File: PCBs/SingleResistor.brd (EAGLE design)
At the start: 14.5 x 42 mm, 3 parts

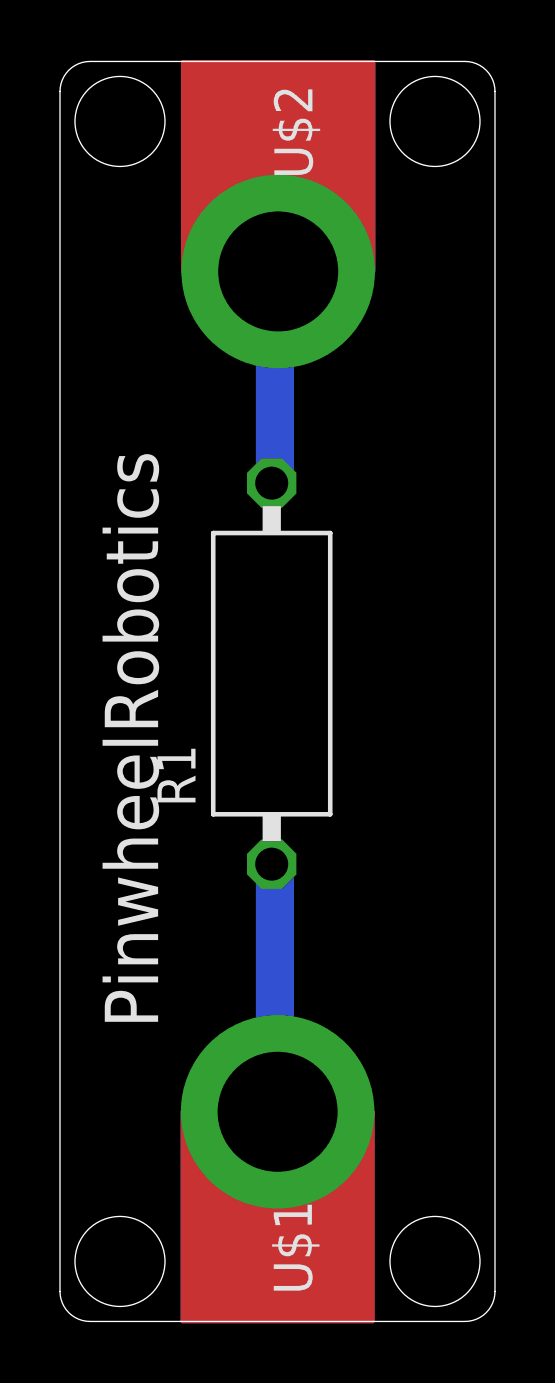
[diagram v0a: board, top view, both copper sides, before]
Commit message: Update for Dim width is 42 length is 28 for type 2 pcb
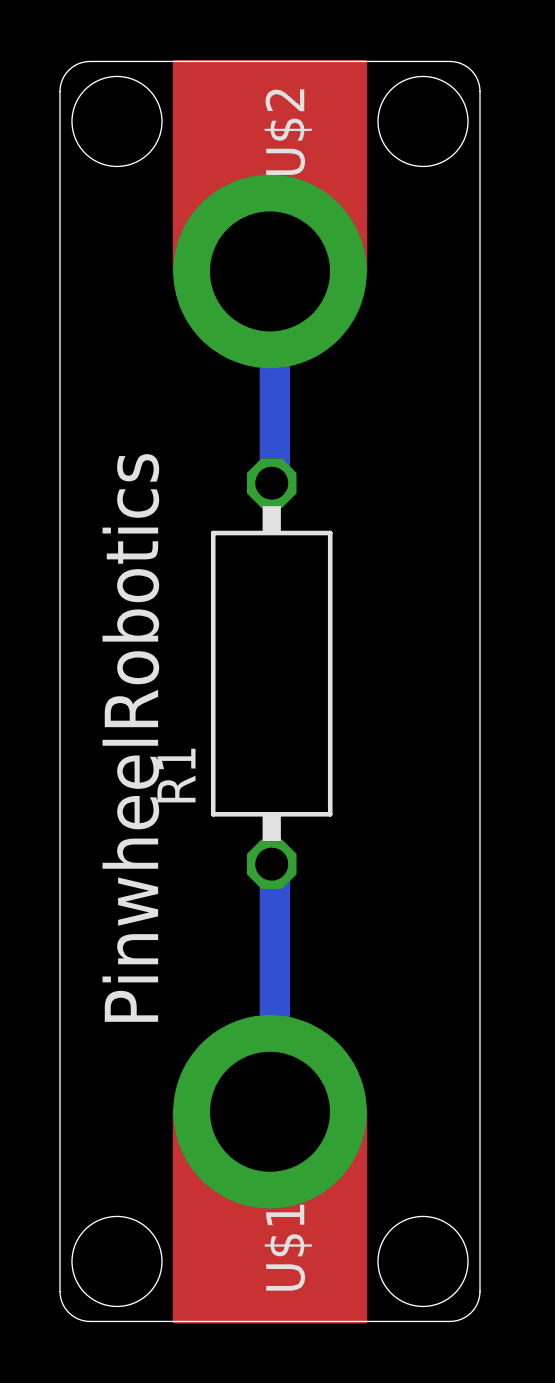
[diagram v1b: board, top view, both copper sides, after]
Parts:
- moved U$2 0.27 mm to (7.00, 35.0)
- moved U$1 0.25 mm to (7.00, 6.99)
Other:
- board size 14.5 x 42 mm -> 14 x 42 mm
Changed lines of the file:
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@@
 <drawing>
 <settings>
-<setting alwaysvectorfont="no"/>
+<setting alwaysvectorfont="yes"/>
 <setting verticaltext="up"/>
 </settings>
@@
 <board>
 <plain>
-<wire x1="1" y1="0" x2="13.5" y2="0" width="0" layer="20"/>
-<wire x1="13.5" y1="0" x2="14.5" y2="1" width="0" layer="20" curve="90"/>
-<wire x1="14.5" y1="1" x2="14.5" y2="41" width="0" layer="20"/>
-<wire x1="14.5" y1="41" x2="13.5" y2="42" width="0" layer="20" curve="90"/>
-<wire x1="13.5" y1="42" x2="1" y2="42" width="0" layer="20"/>
+<wire x1="13" y1="42" x2="1" y2="42" width="0" layer="20"/>
 <wire x1="1" y1="42" x2="0" y2="41" width="0" layer="20" curve="90"/>
 <wire x1="0" y1="41" x2="0" y2="1" width="0" layer="20"/>
 <wire x1="0" y1="1" x2="1" y2="0" width="0" layer="20" curve="90"/>
-<hole x="2" y="40" drill="3"/>
-<hole x="12.5" y="40" drill="3"/>
-<hole x="2" y="2" drill="3"/>
-<hole x="12.5" y="2" drill="3"/>
+<wire x1="1" y1="0" x2="13" y2="0" width="0" layer="20"/>
+<wire x1="13" y1="0" x2="14" y2="1" width="0" layer="20" curve="90"/>
+<wire x1="14" y1="1" x2="14" y2="41" width="0" layer="20"/>
+<wire x1="14" y1="41" x2="13" y2="42" width="0" layer="20" curve="90"/>
+<hole x="1.9" y="40" drill="3"/>
+<hole x="12.1" y="40" drill="3"/>
+<hole x="1.9" y="2" drill="3"/>
+<hole x="12.1" y="2" drill="3"/>
 <text x="3.271" y="9.772" size="1.778" layer="21" rot="R90">PinwheelRobotics</text>
 <text x="12.509" y="29.939" size="1.778" layer="22" rot="MR270">care@pinwheel.in</text>
-<dimension x1="-1" y1="42" x2="-1" y2="0" x3="-2.5" y3="21" textsize="1.778" layer="1"/>
-<dimension x1="0" y1="42.5" x2="14.5" y2="42.5" x3="7.25" y3="44" textsize="1.778" layer="1"/>
 </plain>
 <attributes>
@@
 <attribute name="VALUE" x="7.693" y="17.148" size="1.27" layer="27" ratio="10" rot="R90"/>
 </element>
-<element name="U$2" library="microbit" package="MICROBIT_PAD" value="MICROBIT_PAD" x="7.273" y="35" smashed="yes" rot="R180">
-<attribute name="NAME" x="7.146" y="41.223" size="1.27" layer="21" rot="R270"/>
+<element name="U$2" library="microbit" package="MICROBIT_PAD" value="MICROBIT_PAD" x="7" y="35" smashed="yes" rot="R180">
+<attribute name="NAME" x="6.873" y="41.223" size="1.27" layer="21" rot="R270"/>
 </element>
-<element name="U$1" library="microbit" package="MICROBIT_PAD" value="MICROBIT_PAD" x="7.254" y="6.988" smashed="yes">
-<attribute name="NAME" x="8.397" y="0.892" size="1.27" layer="21" rot="R90"/>
+<element name="U$1" library="microbit" package="MICROBIT_PAD" value="MICROBIT_PAD" x="7" y="6.988" smashed="yes">
+<attribute name="NAME" x="8.143" y="0.892" size="1.27" layer="21" rot="R90"/>
 </element>
 </elements>
@@
 <contactref element="R1" pad="1"/>
 <contactref element="U$1" pad="PAD"/>
-<wire x1="7.1628" y1="7.0104" x2="7.1628" y2="15.24" width="1.27" layer="16"/>
+<wire x1="7.1628" y1="7.0104" x2="7.1628" y2="15.24" width="1.016" layer="16"/>
 <wire x1="7.1628" y1="15.24" x2="7.058" y2="15.243" width="0.1524" layer="16"/>
-<wire x1="7.1628" y1="7.0104" x2="7.254" y2="6.988" width="0.1524" layer="16"/>
+<wire x1="7.1628" y1="7.0104" x2="7" y2="6.988" width="0.1524" layer="16"/>
 </signal>
 <signal name="N$2">
 <contactref element="U$2" pad="PAD"/>
 <contactref element="R1" pad="2"/>
-<wire x1="7.1628" y1="34.8996" x2="7.1628" y2="28.0416" width="1.27" layer="16"/>
+<wire x1="7.1628" y1="34.8996" x2="7.1628" y2="28.0416" width="1.016" layer="16"/>
 <wire x1="7.1628" y1="28.0416" x2="7.058" y2="27.943" width="0.1524" layer="16"/>
-<wire x1="7.1628" y1="34.8996" x2="7.273" y2="35" width="0.1524" layer="16"/>
+<wire x1="7.1628" y1="34.8996" x2="7" y2="35" width="0.1524" layer="16"/>
 </signal>
 </signals>

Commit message: Corrected hole position for some design , made transistor as switch as category 1
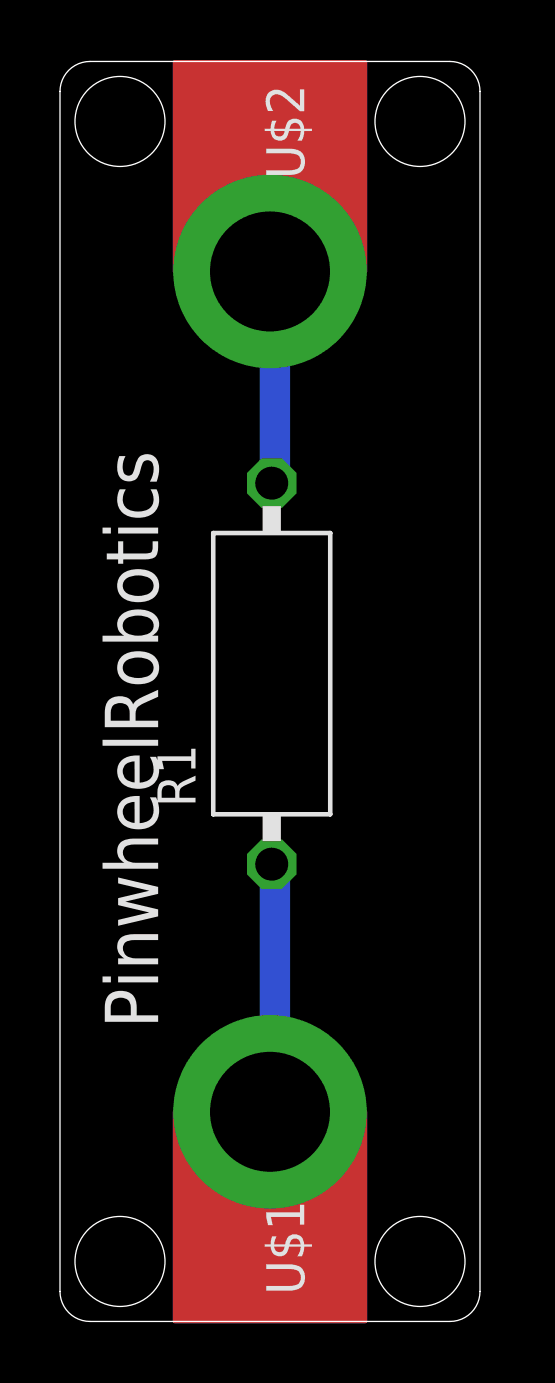
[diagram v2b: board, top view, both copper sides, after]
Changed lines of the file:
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@@
 <drawing>
 <settings>
-<setting alwaysvectorfont="yes"/>
+<setting alwaysvectorfont="no"/>
 <setting verticaltext="up"/>
 </settings>
@@
 <wire x1="14" y1="1" x2="14" y2="41" width="0" layer="20"/>
 <wire x1="14" y1="41" x2="13" y2="42" width="0" layer="20" curve="90"/>
-<hole x="1.9" y="40" drill="3"/>
-<hole x="12.1" y="40" drill="3"/>
-<hole x="1.9" y="2" drill="3"/>
-<hole x="12.1" y="2" drill="3"/>
+<hole x="2" y="40" drill="3"/>
+<hole x="12" y="40" drill="3"/>
+<hole x="2" y="2" drill="3"/>
+<hole x="12" y="2" drill="3"/>
 <text x="3.271" y="9.772" size="1.778" layer="21" rot="R90">PinwheelRobotics</text>
 <text x="12.509" y="29.939" size="1.778" layer="22" rot="MR270">care@pinwheel.in</text>
